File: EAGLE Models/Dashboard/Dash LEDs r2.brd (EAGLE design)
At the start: 61 x 8.3 mm, 7 parts

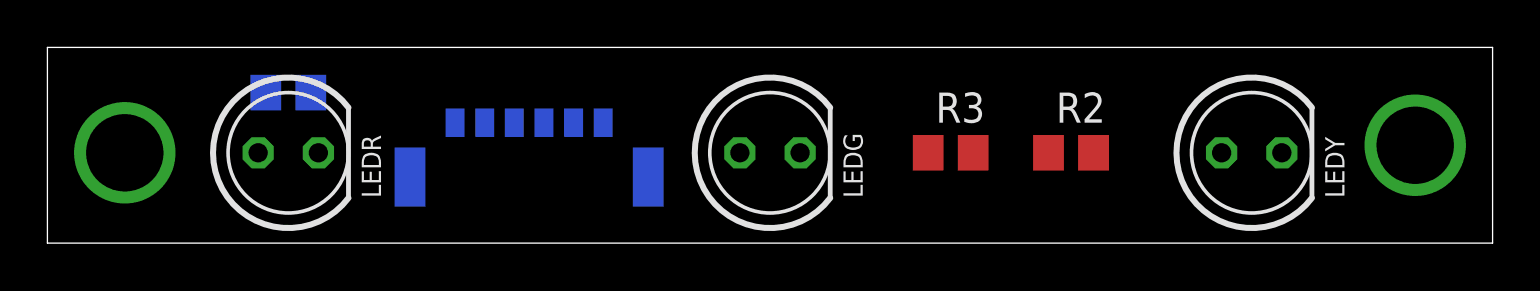
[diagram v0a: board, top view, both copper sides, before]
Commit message: Route Dash LEDs r2 board.
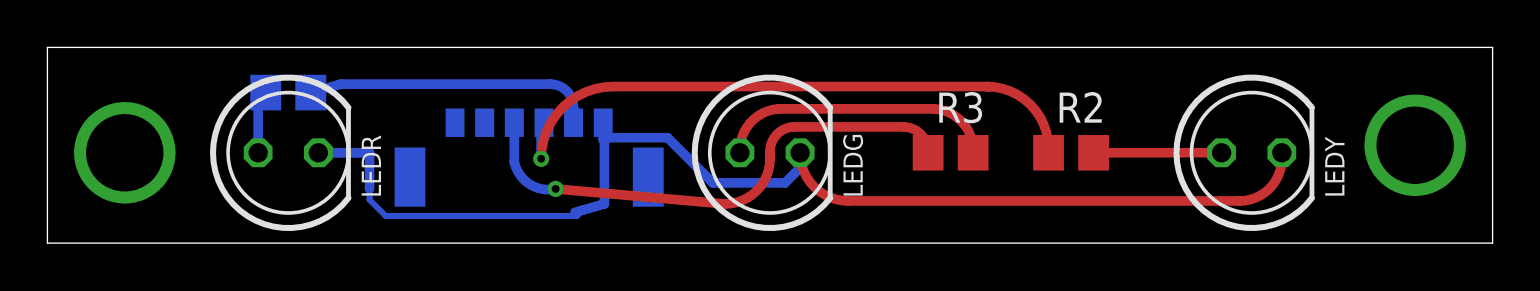
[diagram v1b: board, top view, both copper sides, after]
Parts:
- turned R1 to 0 degrees
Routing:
- net GND: track 0.00 -> 50.4 mm
- net DRV2: track 0.00 -> 25.6 mm, vias 0 -> 1
- net DRV3: track 0.00 -> 21.5 mm, vias 0 -> 1
- net DRV1: track 0.00 -> 12.2 mm
- net N$3: track 0.00 -> 11.5 mm
- net N$2: track 0.00 -> 5.40 mm
- net N$1: track 0.00 -> 2.67 mm

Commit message: Replace connectors with vias for soldering.
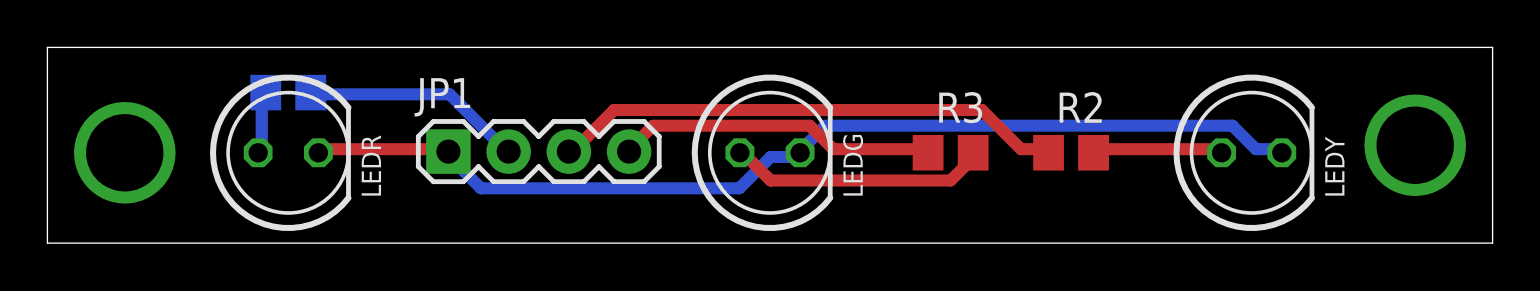
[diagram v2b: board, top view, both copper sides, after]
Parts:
- removed U$1: MICRO6LOCK, DashAndCAN library:MICRO6LOCK
- added JP1: (no value), SparkFun-Connectors:1X04
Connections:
- net DRV1: now also JP1.2; no longer U$1.P2
- net DRV2: now also JP1.3; no longer U$1.P3
- net DRV3: now also JP1.4; no longer U$1.P4
- net GND: now also JP1.1; no longer U$1.P1
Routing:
- net DRV3: track 21.5 -> 13.6 mm, vias 1 -> 0
- net GND: track 50.4 -> 43.0 mm
- net DRV2: track 25.6 -> 21.7 mm, vias 1 -> 0
- net DRV1: track 12.2 -> 9.34 mm
- net N$3: track 11.5 -> 11.0 mm
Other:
- board text added: "G"
- board text added: "GND"
- board text added: "R"
- board text added: "Y"
